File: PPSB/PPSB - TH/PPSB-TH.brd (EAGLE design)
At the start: 20.3 x 25.1 mm, 4 parts, among them K1 ARK500/3

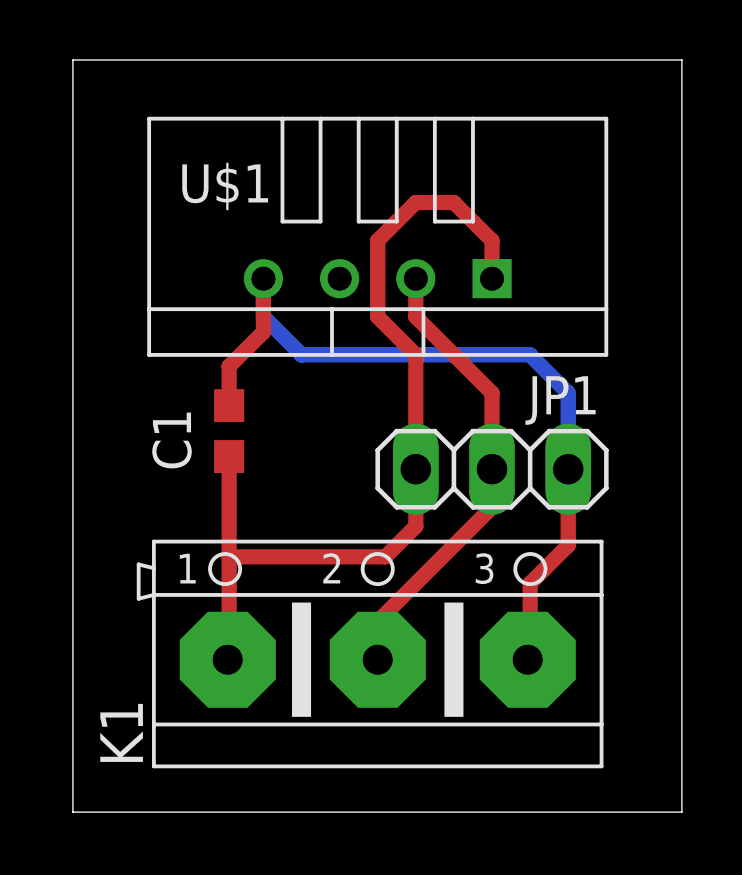
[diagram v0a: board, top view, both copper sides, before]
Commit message: Remove obsolete files, pre-release versions of PPSB-T & PPSB-TH
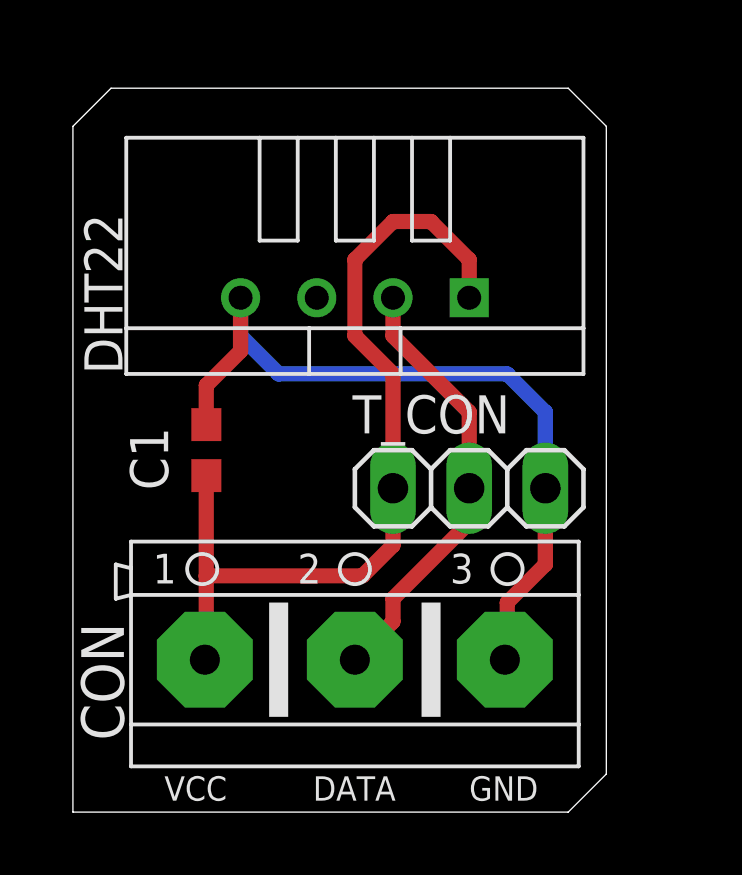
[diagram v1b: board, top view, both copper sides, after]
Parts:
- removed JP1: (no value), pinhead:1X03
- removed K1: ARK500/3, #PaJa_konektory:ARK500/3
- removed U$1: DHT22, diy-modules:TEMP-HUM-SENSOR-DHT22
- added CON: ARK500/3, #PaJa_konektory:ARK500/3
- added DHT22: DHT22, diy-modules:TEMP-HUM-SENSOR-DHT22
- added T_CON: (no value), pinhead:1X03
- moved C1 0.99 mm to (4.45, 12.1)
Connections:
- net +5V: now also CON.1, DHT22.1, T_CON.1; no longer JP1.1, K1.1, U$1.1
- net DATA_OUT: now also CON.2, DHT22.2, T_CON.2; no longer JP1.2, K1.2, U$1.2
- net GND: now also CON.3, DHT22.4, T_CON.3; no longer JP1.3, K1.3, U$1.4
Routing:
- net DATA_OUT: track 15.3 -> 14.7 mm
- net GND: track 26.6 -> 26.0 mm
- net +5V: track 29.6 -> 29.0 mm
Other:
- board size 20.3 x 25.1 mm -> 17.8 x 24.1 mm
- board text added: "DATA"
- board text added: "GND"
- board text added: "VCC"
